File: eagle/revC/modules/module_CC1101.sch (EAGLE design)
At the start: 14 parts, among them X1 734120110

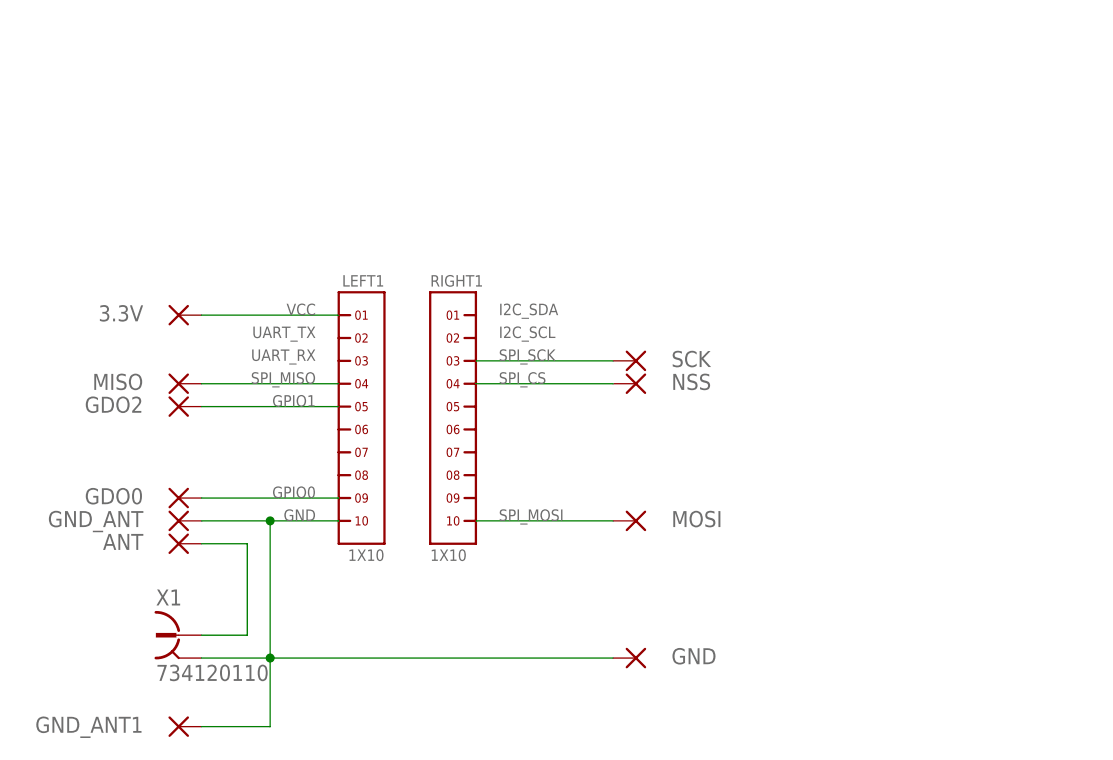
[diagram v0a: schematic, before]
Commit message: Replaced modules with library parts
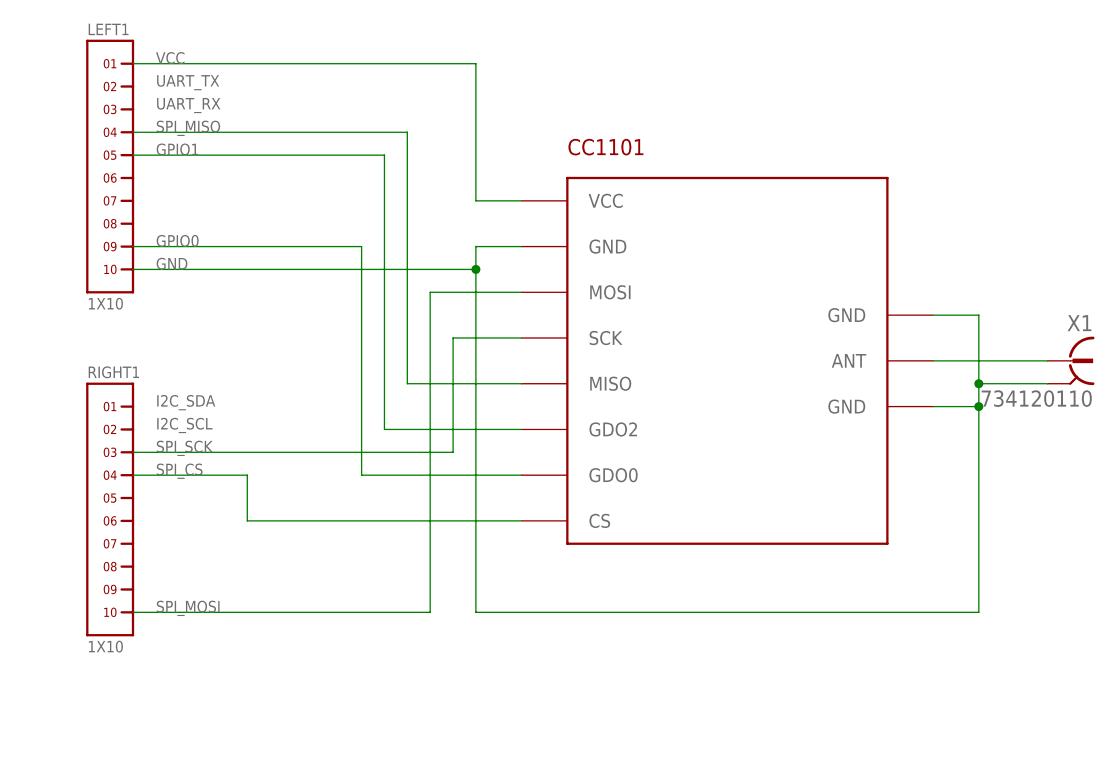
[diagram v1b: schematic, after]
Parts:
- removed 3.3V, ANT, GDO0, GDO2, GND, GND_ANT, GND_ANT1, MISO, MOSI, NSS, SCK: (no value), wirepad:SMD2
- added CC1101: CC1101, RadioShield:CC1101
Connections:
- removed net ANT: ANT.P, X1.1
- new net N$1: CC1101.ANT, X1.1
- net GND: now also CC1101.GND@1, CC1101.GND@2, CC1101.GND@3; no longer GND.P, GND_ANT.P, GND_ANT1.P
- net INT0: now also CC1101.GDO0; no longer GDO0.P
- net INT1: now also CC1101.GDO2; no longer GDO2.P
- net SPI_CS: now also CC1101.CS; no longer NSS.P
- net SPI_MISO: now also CC1101.MISO; no longer MISO.P
- net SPI_MOSI: now also CC1101.MOSI; no longer MOSI.P
- net SPI_SCK: now also CC1101.SCK; no longer SCK.P
- net VCC: now also CC1101.VCC; no longer 3.3V.P
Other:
- moved on the sheet: LEFT1, RIGHT1, X1
